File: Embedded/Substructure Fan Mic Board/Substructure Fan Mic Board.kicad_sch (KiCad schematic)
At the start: 11 parts, among them J1 Conn_01x03_Socket, J2 Conn_01x02_Socket, J3 Conn_01x02_Socket, Q1 DMG3402L, Q2 DMG3402L, U2 F FFC

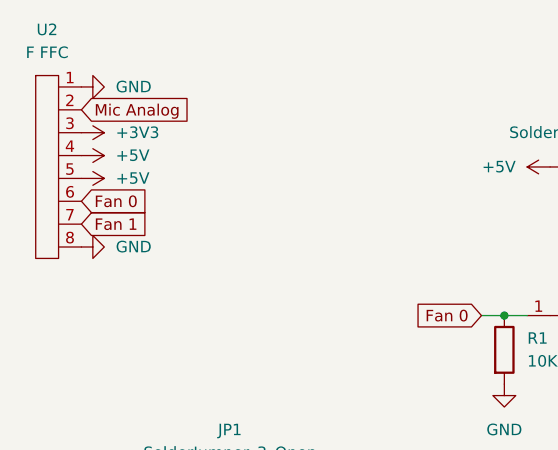
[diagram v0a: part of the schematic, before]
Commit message: Modified Ports to fit FFC orientations
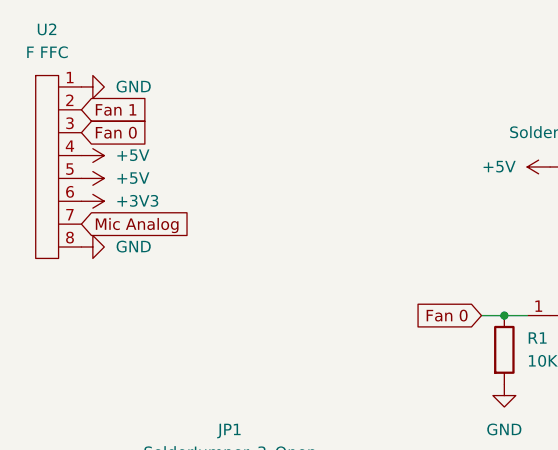
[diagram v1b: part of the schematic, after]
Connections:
- net +3V3: now also U2.6; no longer U2.3
- net Fan 0: now also U2.3; no longer U2.6
- net Fan 1: now also U2.2; no longer U2.7
- net Mic Analog: now also U2.7; no longer U2.2
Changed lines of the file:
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@@
 	(global_label "Fan 0"
 		(shape input)
-		(at 29.21 50.8 0)
+		(at 29.21 43.18 0)
 		(fields_autoplaced yes)
 		(effects
@@
 		)
 		(property "Intersheetrefs" "${INTERSHEET_REFS}"
-			(at 37.7589 50.8 0)
+			(at 37.7589 43.18 0)
 			(effects
 				(font
@@
 	(global_label "Fan 1"
 		(shape input)
-		(at 29.21 53.34 0)
+		(at 29.21 40.64 0)
 		(fields_autoplaced yes)
 		(effects
@@
 		)
 		(property "Intersheetrefs" "${INTERSHEET_REFS}"
-			(at 37.7589 53.34 0)
+			(at 37.7589 40.64 0)
 			(effects
 				(font
@@
 	(global_label "Mic Analog"
 		(shape input)
-		(at 29.21 40.64 0)
+		(at 29.21 53.34 0)
 		(fields_autoplaced yes)
 		(effects
@@
 		)
 		(property "Intersheetrefs" "${INTERSHEET_REFS}"
-			(at 42.6574 40.64 0)
+			(at 42.6574 53.34 0)
 			(effects
 				(font
@@
 	(symbol
 		(lib_id "power:+3V3")
-		(at 29.21 43.18 270)
+		(at 29.21 50.8 270)
+		(mirror x)
 		(unit 1)
 		(exclude_from_sim no)
@@
 		(fields_autoplaced yes)
 		(property "Reference" "#PWR06"
-			(at 25.4 43.18 0)
+			(at 25.4 50.8 0)
 			(effects
 				(font
@@
 		)
 		(property "Value" "+3V3"
-			(at 33.02 43.1799 90)
+			(at 33.02 50.8001 90)
 			(effects
 				(font
@@
 		)
 		(property "Footprint" ""
-			(at 29.21 43.18 0)
+			(at 29.21 50.8 0)
 			(effects
 				(font
@@
 		)
 		(property "Datasheet" ""
-			(at 29.21 43.18 0)
+			(at 29.21 50.8 0)
 			(effects
 				(font
@@
 		)
 		(property "Description" "Power symbol creates a global label with name \"+3V3\""
-			(at 29.21 43.18 0)
-			(effects
-				(font
+			(at 29.21 50.8 0)
+			(effects
+				(font
